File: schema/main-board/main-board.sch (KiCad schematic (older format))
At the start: 14 parts

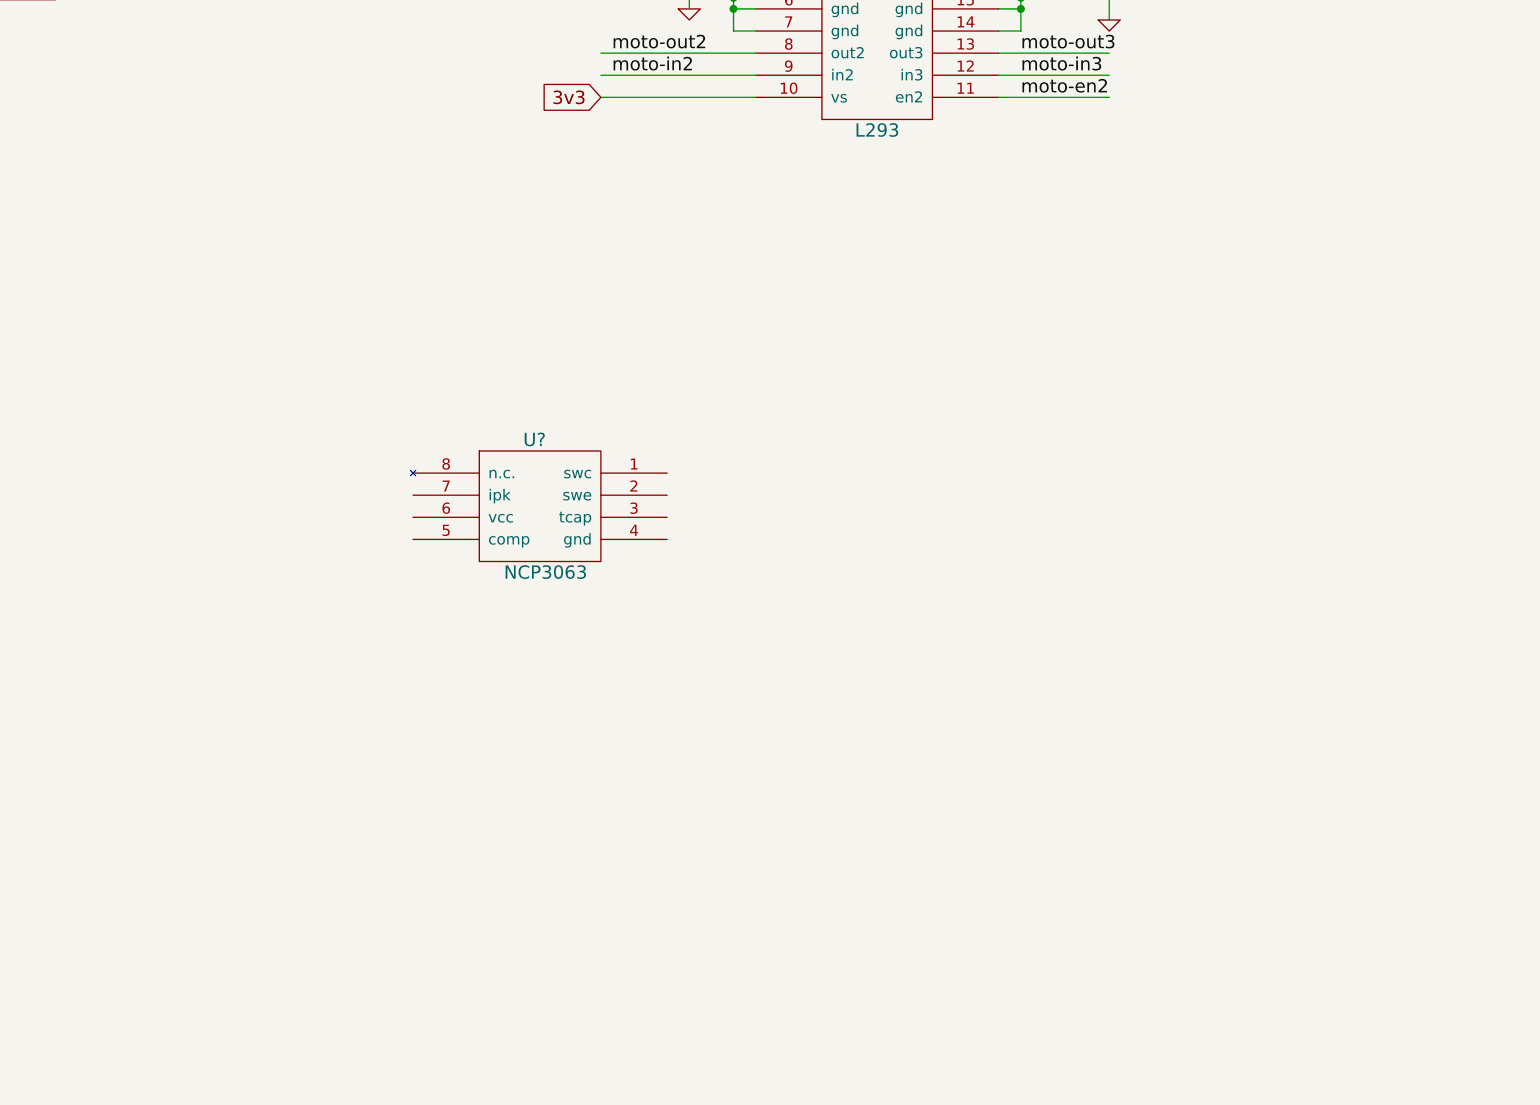
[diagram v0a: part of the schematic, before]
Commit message: Buck circuit development.
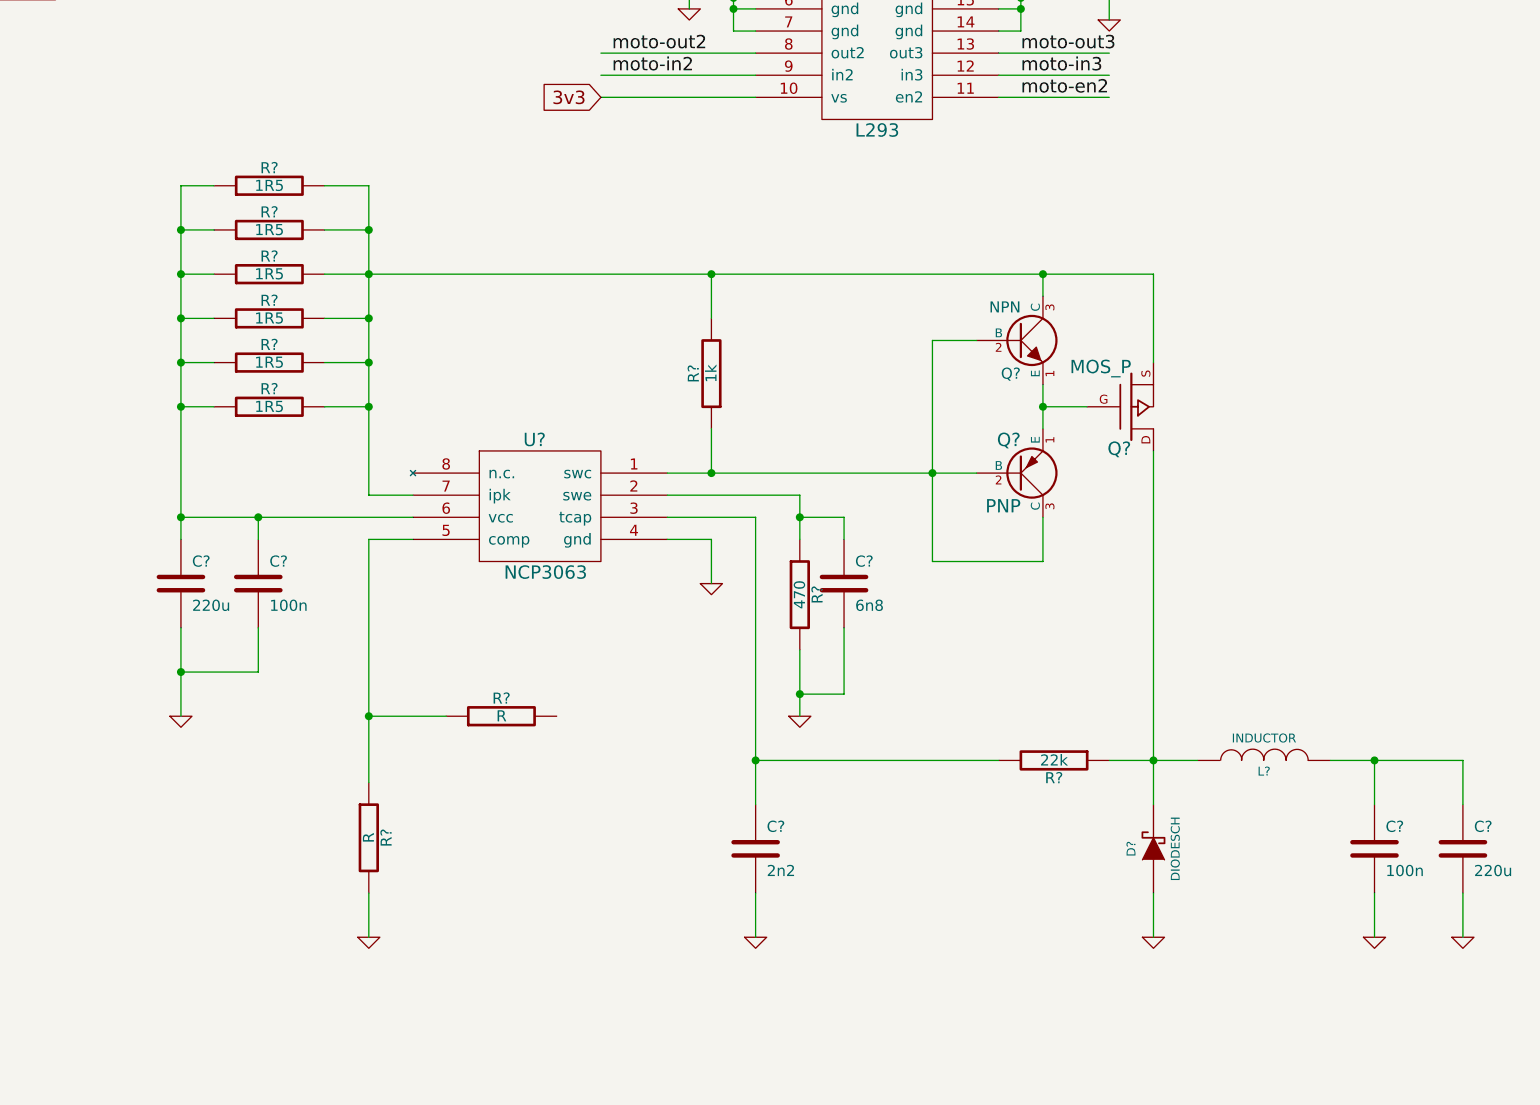
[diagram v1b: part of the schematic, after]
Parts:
- added C? (x2): 220u, symbol C
- added C? (x2): 100n, symbol C
- added C?: 2n2, symbol C
- added C?: 6n8, symbol C
- added D?: DIODESCH, symbol DIODESCH
- added L?: INDUCTOR, symbol INDUCTOR
- added Q?: NPN, symbol NPN
- added Q?: PNP, symbol PNP
- added Q?: MOS_P, symbol MOS_P
- added R? (x2): R, symbol R
- added R?: 1k, symbol R
- added R? (x6): 1R5, symbol R
- added R?: 22k, symbol R
- added R?: 470, symbol R
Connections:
- wire segments 48 -> 104

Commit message: Added LED power source with current limit.
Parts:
- added C? (x2): 100n, symbol C
- added C? (x2): 220u, symbol C
- added C?: 2n2, symbol C
- added D?: 1N5819, symbol DIODESCH
- added L? (x2): 10u, symbol INDUCTOR
- added P? (x5): TST, symbol TST
- added Q? (x2): MOS_N, symbol MOS_N
- added Q?: si2301, symbol MOS_P
- added R? (x2): 1k, symbol R
- added R? (x6): 1R5, symbol R
- added R? (x2): R, symbol R
- added U?: NCP3063, symbol NCP3063
- D?: value DIODESCH -> 1N5819
- L?: value INDUCTOR -> 10u
- Q?: value MOS_P -> si2301
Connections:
- net labels added: 5v, buck-en, gnd-5v, led, led-en, led-gnd
- wire segments 104 -> 168
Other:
- moved on the sheet: C?, D?, L?, P?, Q?, R?, U?

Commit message: Schematic finished or looks like more or less finished.
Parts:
- removed P? (x4): TST, symbol TST
- added P10, P7, P8, P9: TST, symbol TST
- added P11: CONN_20, symbol CONN_20
- added P12, P13, P14: CONN_4, symbol CONN_4
- added R10, R8: 10k, symbol R
- Q1, Q2: renamed from Q?; value MOS_N -> irll2703
- R23, R24, R25: renamed from R?; value R -> 10k
- R26: renamed from R?; value R -> 30k
- gave numbers to parts that had none: 53
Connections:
- net labels added: moto-en, scl, sda
- net labels removed: moto-en1, moto-en2
- wire segments 168 -> 218
- no-connect marks 0 -> 5
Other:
- note added: "This is for an MCU board attach"
- note added: "This is for attaching solar panel."
- note added: "This is in order to have an I2C \nbus on a main-board."

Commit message: For onboard computer changed to P-channel MOSFETS in order to make MCU board GND to be the same as computer's GND.
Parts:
- removed Q2: irll2703, symbol MOS_N
- added C7, C8: 2n2, symbol C
- added Q1: bc847, symbol NPN
- added Q2, Q3: si2301, symbol MOS_P
- added R1, R8: 10k, symbol R
- C6: renamed from C7; value 6n8 -> 2n2
- Q5: renamed from Q3; value NPN -> bc847
- Q6: renamed from Q4; value PNP -> bc857
- renumbered C3 to C1, C8 to C12, C9 to C13, C4 to C2, C1 to C3, C5 to C4, C2 to C5, C6 to C9, D2 to D1, D1 to D2, L2 to L1, L3 to L2, L1 to L3, P6 to P10, P7 to P3, P8 to P4, P9 to P5, P10 to P6, P3 to P7, P4 to P8, P5 to P9, Q1 to Q4, Q5 to Q7, Q6 to Q8, R17 to R11, R18 to R12, R19 to R13, R20 to R14, R21 to R15, R22 to R16, R8 to R17, R24 to R18, R7 to R19, R1 to R2, R26 to R20, R27 to R21, R28 to R22, R11 to R23, R12 to R24, R13 to R25, R14 to R26, R15 to R27, R16 to R28, R23 to R29, R2 to R3, R25 to R30, R29 to R31, R3 to R4, R4 to R5, R5 to R6, R6 to R7, U3 to U2, U2 to U3
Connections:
- net labels removed: gnd-5v
- wire segments 218 -> 231
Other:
- note added: "Here it should be 6n8\ne.i. approximately \n3 x 2n2."
- note added: "Here it's right.\nBit C to Gnd \ndirectly."
- moved on the sheet: C1, C10, C11, C2, C4, C6, D1, L1, L2, P1, P11, P12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
